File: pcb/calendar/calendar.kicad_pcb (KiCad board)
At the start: 4 copper layers, 41.1 x 30.1 mm, 10 parts, among them J1 INP, J2 Conn_02x06_Odd_Even, J3 Conn_02x05_Odd_Even, U1 PCF8563T, U2 MAX7219, Y1 32 768

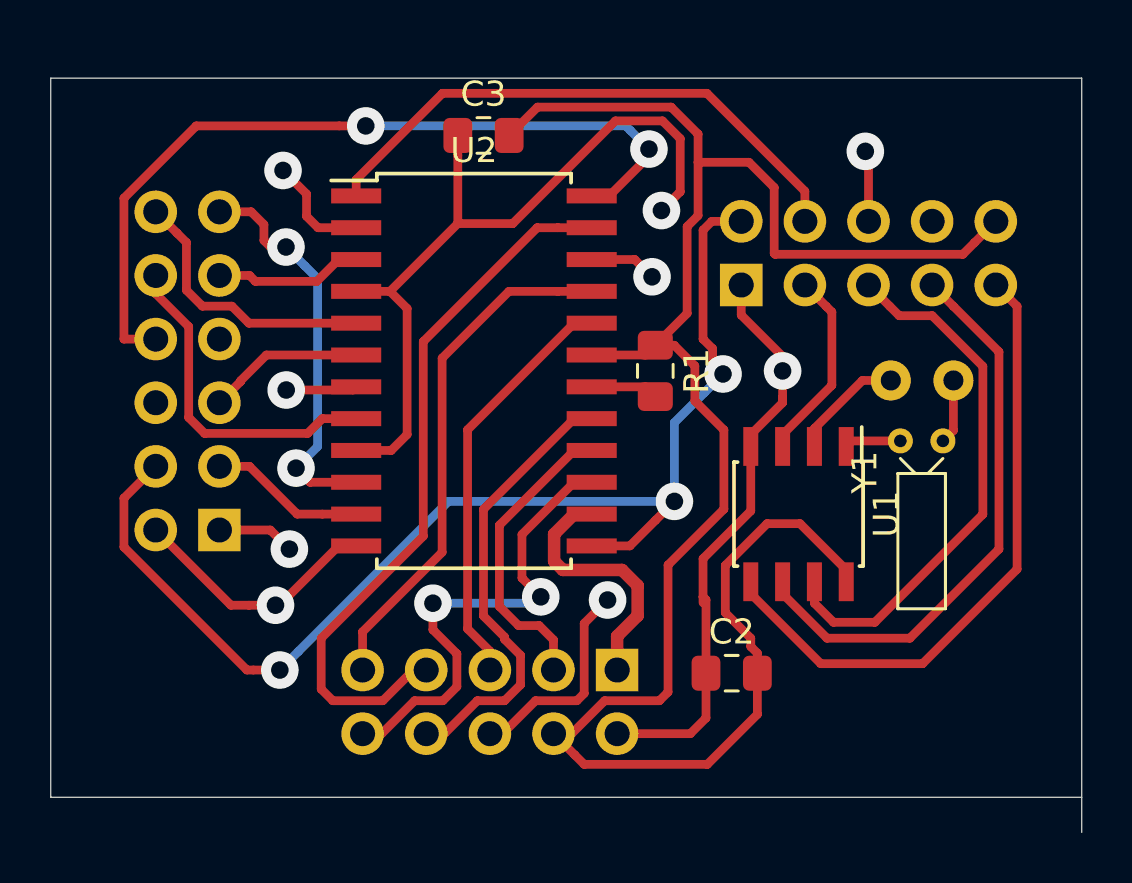
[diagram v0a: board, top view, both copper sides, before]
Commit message: Moved pins around eliminating vias.
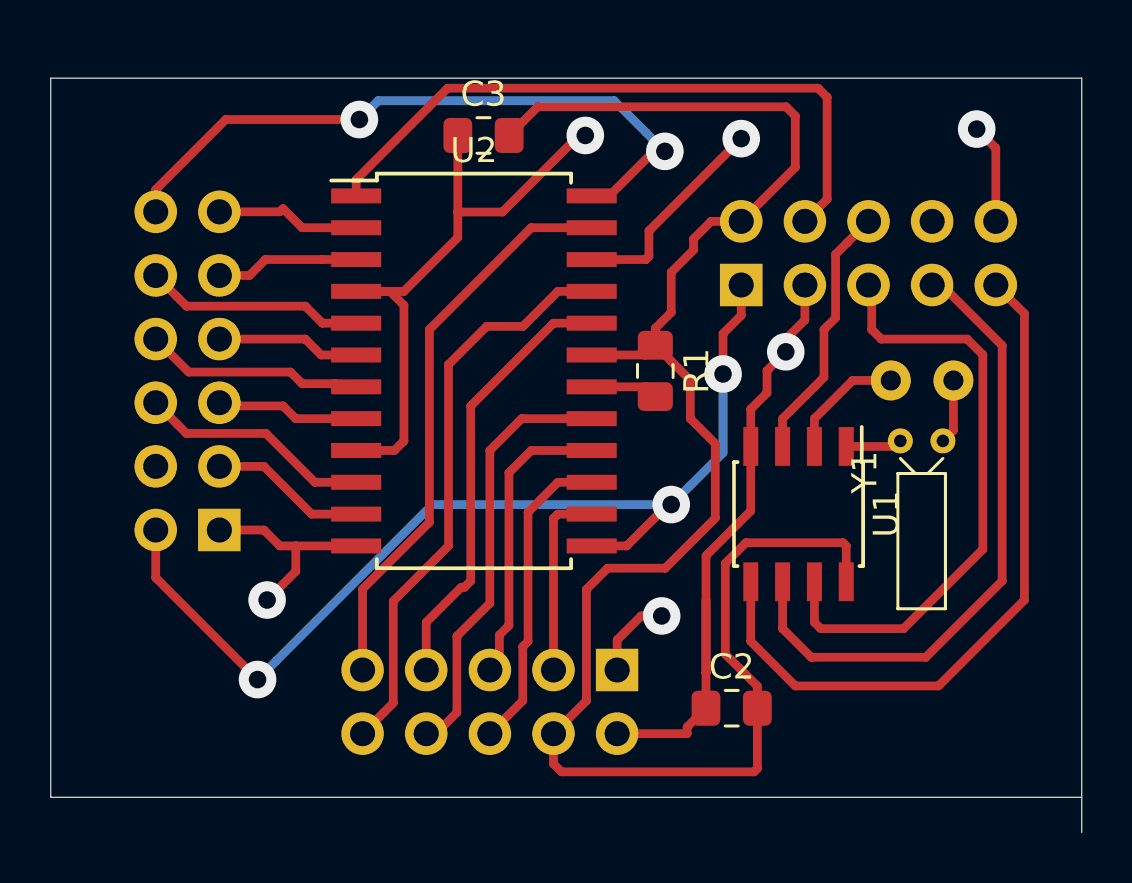
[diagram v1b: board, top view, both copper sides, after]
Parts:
- moved C2 1.40 mm to (80.4, 67.7)
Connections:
- J1 pad 1: GND -> SCLK
- J1 pad 10: +5V -> LOAD
- J1 pad 2: SCLK -> +5V
- J1 pad 3: T~INT -> GND
- J1 pad 6: LOAD -> T~INT
- J2 pad 1: D0 -> LOAD
- J2 pad 10: D7 -> D6
- J2 pad 11: D5 -> D0
- J2 pad 12: D6 -> DOUT
- J2 pad 2: LOAD -> SCLK
- J2 pad 4: SCLK -> (no net)
- J2 pad 5: D2 -> D7
- J2 pad 6: (no net) -> D5
- J2 pad 7: D3 -> D2
- J2 pad 8: DOUT -> D3
- J3 pad 1: A -> DP
- J3 pad 10: F -> E
- J3 pad 3: B -> A
- J3 pad 5: C -> B
- J3 pad 6: DP -> F
- J3 pad 7: D -> C
- J3 pad 9: E -> D
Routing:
- net D0: track 23.5 -> 5.83 mm, vias 2 -> 0
- net DP: track 25.2 -> 34.1 mm
- net D7: track 13.4 -> 5.72 mm
- net +5V: track 80.1 -> 72.6 mm
- net SCLK: track 48.2 -> 40.8 mm
- net D5: track 16.0 -> 9.32 mm, vias 2 -> 0
- net F: track 19.1 -> 12.5 mm, vias 2 -> 0
- net D: track 29.1 -> 22.9 mm
- net DOUT: track 32.7 -> 27.2 mm
- net LOAD: track 45.9 -> 50.3 mm
- net DIN: track 22.8 -> 26.4 mm
- net SDA: track 25.5 -> 28.5 mm
- net A: track 10.4 -> 7.65 mm
- net TCLK: track 21.5 -> 24.2 mm
- net T~INT: track 7.71 -> 10.4 mm
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
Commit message: New pcb
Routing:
- net +5V: track 72.6 -> 73.2 mm
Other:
- board size 41.1 x 30.1 mm -> 41.1 x 28.7 mm

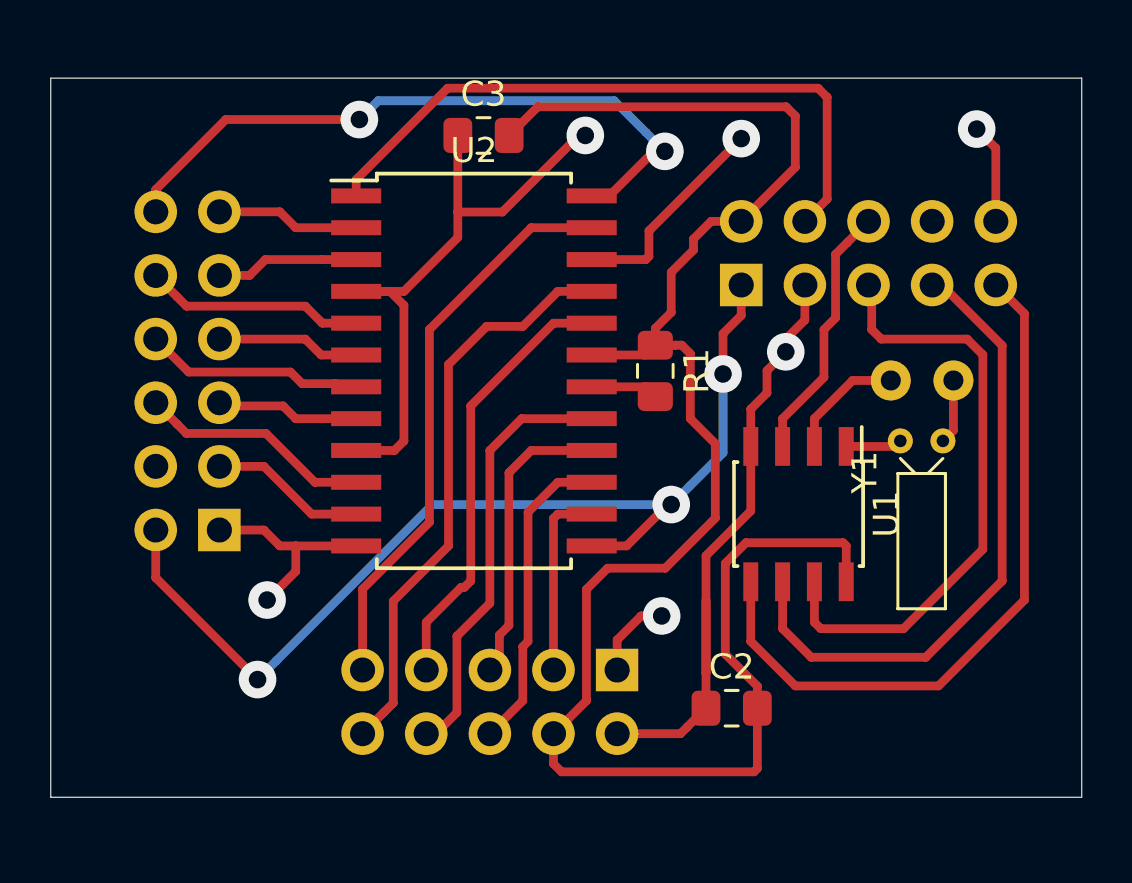
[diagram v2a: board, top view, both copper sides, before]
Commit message: Changed from pins to wire rings.
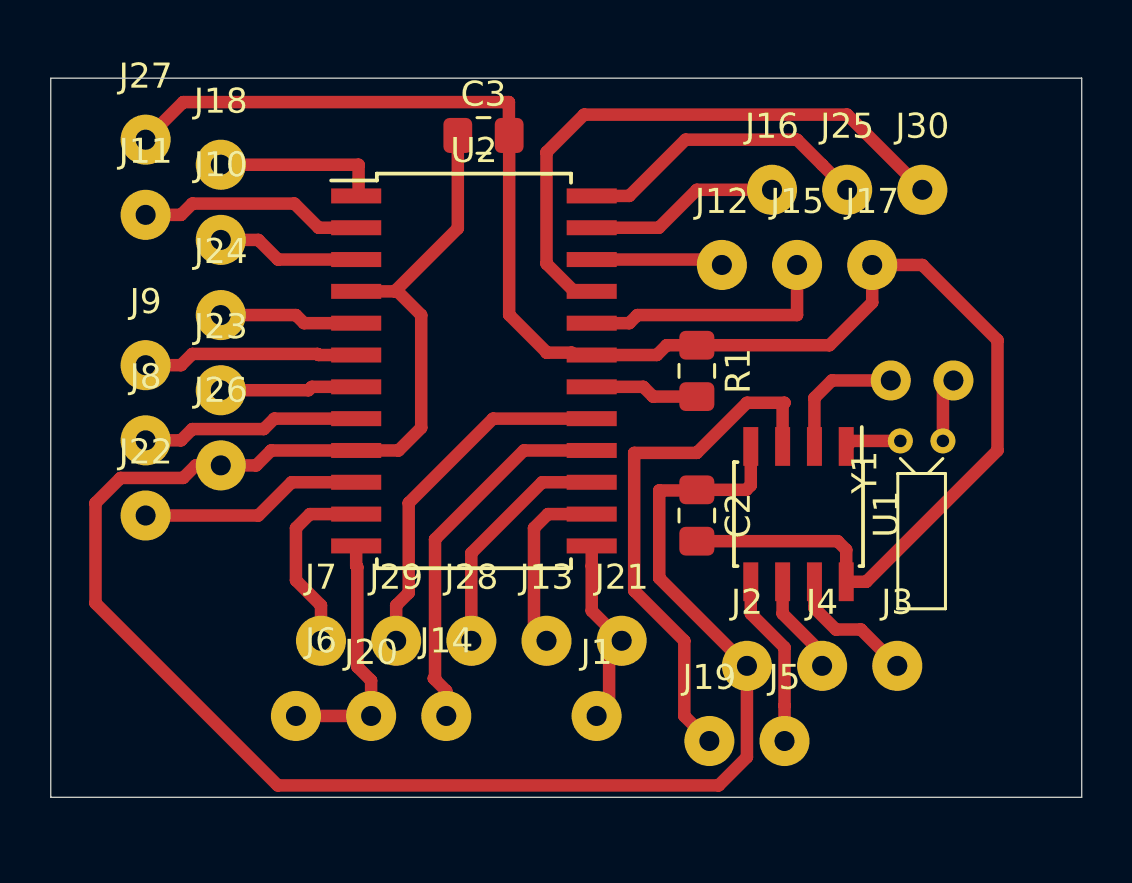
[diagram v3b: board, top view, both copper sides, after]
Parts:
- added J10: J, Connector_Wire:SolderWirePad_1x01_Drill0.8mm, F.Cu at (60.0, 49.0)
- added J11: J, Connector_Wire:SolderWirePad_1x01_Drill0.8mm, F.Cu at (57.0, 48.0)
- added J12: J, Connector_Wire:SolderWirePad_1x01_Drill0.8mm, F.Cu at (80.0, 50.0)
- added J13: J, Connector_Wire:SolderWirePad_1x01_Drill0.8mm, F.Cu at (73.0, 65.0)
- added J14: J, Connector_Wire:SolderWirePad_1x01_Drill0.8mm, F.Cu at (69.0, 68.0)
- added J15: J, Connector_Wire:SolderWirePad_1x01_Drill0.8mm, F.Cu at (83.0, 50.0)
- added J16: J, Connector_Wire:SolderWirePad_1x01_Drill0.8mm, F.Cu at (82.0, 47.0)
- added J17: J, Connector_Wire:SolderWirePad_1x01_Drill0.8mm, F.Cu at (86.0, 50.0)
- added J18: J, Connector_Wire:SolderWirePad_1x01_Drill0.8mm, F.Cu at (60.0, 46.0)
- added J19: J, Connector_Wire:SolderWirePad_1x01_Drill0.8mm, F.Cu at (79.5, 69.0)
- added J20: J, Connector_Wire:SolderWirePad_1x01_Drill0.8mm, F.Cu at (66.0, 68.0)
- added J21: J, Connector_Wire:SolderWirePad_1x01_Drill0.8mm, F.Cu at (76.0, 65.0)
- added J22: J, Connector_Wire:SolderWirePad_1x01_Drill0.8mm, F.Cu at (57.0, 60.0)
- added J23: J, Connector_Wire:SolderWirePad_1x01_Drill0.8mm, F.Cu at (60.0, 55.0)
- added J24: J, Connector_Wire:SolderWirePad_1x01_Drill0.8mm, F.Cu at (60.0, 52.0)
- added J25: J, Connector_Wire:SolderWirePad_1x01_Drill0.8mm, F.Cu at (85.0, 47.0)
- added J26: J, Connector_Wire:SolderWirePad_1x01_Drill0.8mm, F.Cu at (60.0, 58.0)
- added J27: J, Connector_Wire:SolderWirePad_1x01_Drill0.8mm, F.Cu at (57.0, 45.0)
- added J28: J, Connector_Wire:SolderWirePad_1x01_Drill0.8mm, F.Cu at (70.0, 65.0)
- added J29: J, Connector_Wire:SolderWirePad_1x01_Drill0.8mm, F.Cu at (67.0, 65.0)
- added J30: J, Connector_Wire:SolderWirePad_1x01_Drill0.8mm, F.Cu at (88.0, 47.0)
- added J4: J, Connector_Wire:SolderWirePad_1x01_Drill0.8mm, F.Cu at (84.0, 66.0)
- added J5: J, Connector_Wire:SolderWirePad_1x01_Drill0.8mm, F.Cu at (82.5, 69.0)
- added J6: J, Connector_Wire:SolderWirePad_1x01_Drill0.8mm, F.Cu at (63.0, 68.0)
- added J7: J, Connector_Wire:SolderWirePad_1x01_Drill0.8mm, F.Cu at (64.0, 65.0)
- added J8: J, Connector_Wire:SolderWirePad_1x01_Drill0.8mm, F.Cu at (57.0, 57.0)
- added J9: J, Connector_Wire:SolderWirePad_1x01_Drill0.8mm, F.Cu at (57.0, 54.0)
- J1: value INP -> J; footprint Connector_PinSocket_2.54mm:PinSocket_2x05_P2.54mm_Vertical -> Connector_Wire:SolderWirePad_1x01_Drill0.8mm; moved to F.Cu
- J2: value Conn_02x06_Odd_Even -> J; footprint Connector_PinSocket_2.54mm:PinSocket_2x06_P2.54mm_Vertical -> Connector_Wire:SolderWirePad_1x01_Drill0.8mm; moved to F.Cu
- J3: value Conn_02x05_Odd_Even -> J; footprint Connector_PinSocket_2.54mm:PinSocket_2x05_P2.54mm_Vertical -> Connector_Wire:SolderWirePad_1x01_Drill0.8mm; moved to F.Cu
- moved J2 21.7 mm to (81.0, 66.0)
- moved J1 18.1 mm to (75.0, 68.0), turned to 0 degrees
- moved J3 11.2 mm to (87.0, 66.0), turned to 0 degrees
- moved C2 7.82 mm to (79.0, 60.0), turned to 270 degrees
- moved R1 1.66 mm to (79.0, 54.2)
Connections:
- J2 pad 1: LOAD -> GND
- J3 pad 1: DP -> TCLK
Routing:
- net LOAD: track 50.3 -> 10.0 mm, vias 2 -> 0
- net SCLK: track 40.8 -> 7.70 mm, vias 3 -> 0
- net DP: track 34.1 -> 5.29 mm, vias 2 -> 0
- net SDA: track 28.5 -> 6.91 mm
- net SCL: track 25.6 -> 4.01 mm
- net DIN: track 26.4 -> 6.78 mm
- net TCLK: track 24.2 -> 5.31 mm
- net GND: track 63.9 -> 79.8 mm, vias 2 -> 0
- net DOUT: track 27.2 -> 12.0 mm, vias 2 -> 0
- net D: track 22.9 -> 7.82 mm
- net T~INT: track 10.4 -> 21.3 mm
- net C: track 17.5 -> 10.3 mm
- net +5V: track 73.2 -> 67.4 mm
- net D3: track 8.79 -> 5.46 mm
- net D0: track 5.72 -> 8.99 mm
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
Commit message: Moved oints around
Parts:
- moved J20 9.22 mm to (60.0, 61.0)
- moved J7 8.60 mm to (57.0, 60.0)
- moved J26 7.62 mm to (57.0, 51.0)
- moved J22 3.61 mm to (60.0, 58.0)
- moved J6 3.16 mm to (64.0, 65.0)
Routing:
- net GND: track 79.8 -> 87.9 mm
- net D5: track 8.95 -> 5.84 mm
- net D1: track 7.55 -> 8.83 mm
